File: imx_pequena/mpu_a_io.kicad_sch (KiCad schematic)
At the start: 12 parts, among them J1 Conn_ARM_JTAG_SWD_10, U1 MCIMX6Z0DVM09AB, Y1 Crystal, Y2 Crystal

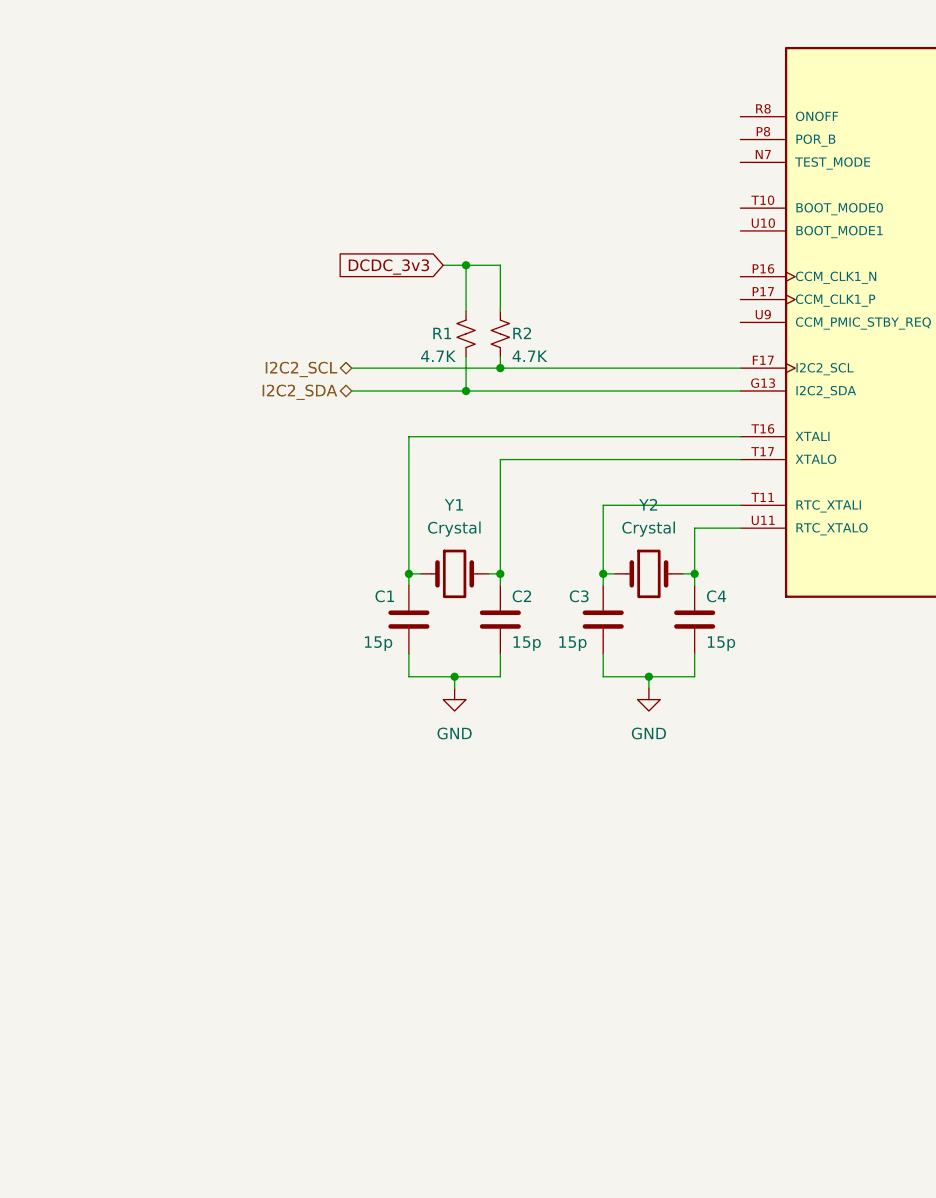
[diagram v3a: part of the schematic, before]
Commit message: Updated config
Updated config file and some pins
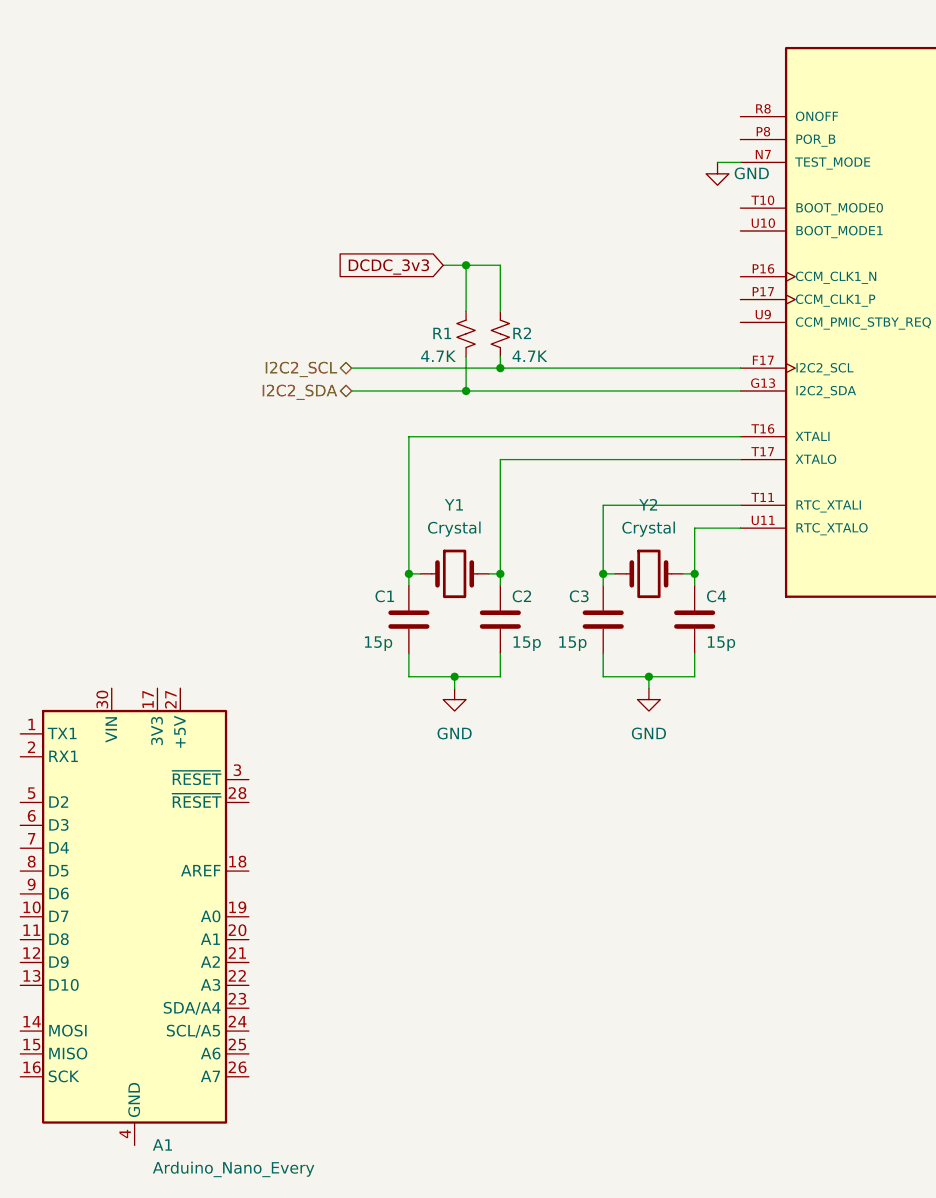
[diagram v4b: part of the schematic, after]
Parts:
- added A1: Arduino_Nano_Every, Module:Arduino_Nano, symbol MCU_Module:Arduino_Nano_Every
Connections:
- net GND: now also U1.N7 (TEST_MODE)
- new net: A1.29 (GND), A1.4 (GND)
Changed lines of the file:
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@@
+    (stroke (width 0) (type default) (color 0 0 0 0))
+  )
+  (wire (pts (xy 106.68 68.58) (xy 109.22 68.58))
     (stroke (width 0) (type default) (color 0 0 0 0))
   )
@@
     (pin "1")
     (pin "2")
+  )
+  (symbol (lib_id "MCU_Module:Arduino_Nano_Every") (at 41.91 152.4 0) (unit 1)
+    (in_bom yes) (on_board yes) (fields_autoplaced)
+    (property "Reference" "A1" (id 0) (at 43.9294 177.8 0)
+      (effects (font (size 1.27 1.27)) (justify left))
+    )
+    (property "Value" "Arduino_Nano_Every" (id 1) (at 43.9294 180.34 0)
+      (effects (font (size 1.27 1.27)) (justify left))
+    )
+    (property "Footprint" "Module:Arduino_Nano" (id 2) (at 41.91 152.4 0)
+      (effects (font (size 1.27 1.27) italic) hide)
+    )
+    (property "Datasheet" "https://content.arduino.cc/assets/NANOEveryV3.0_sch.pdf" (id 3) (at 41.91 152.4 0)
+      (effects (font (size 1.27 1.27)) hide)
+    )
+    (pin "1")
+    (pin "10")
+    (pin "11")
+    (pin "12")
+    (pin "13")
+    (pin "14")
+    (pin "15")
+    (pin "16")
+    (pin "17")
+    (pin "18")
+    (pin "19")
+    (pin "2")
+    (pin "20")
+    (pin "21")
+    (pin "22")
+    (pin "23")
+    (pin "24")
+    (pin "25")
+    (pin "26")
+    (pin "27")
+    (pin "28")
+    (pin "29")
+    (pin "3")
+    (pin "30")
+    (pin "4")
+    (pin "5")
+    (pin "6")
+    (pin "7")
+    (pin "8")
+    (pin "9")
   )
   (symbol (lib_id "power:GND") (at 77.47 127 0) (unit 1)
@@
     (pin "U9")
   )
+  (symbol (lib_id "power:GND") (at 106.68 68.58 0) (unit 1)
+    (in_bom yes) (on_board yes)
+    (property "Reference" "#PWR?" (id 0) (at 106.68 74.93 0)
+      (effects (font (size 1.27 1.27)) hide)
+    )
+    (property "Value" "GND" (id 1) (at 110.49 69.85 0))
+    (property "Footprint" "" (id 2) (at 106.68 68.58 0)
+      (effects (font (size 1.27 1.27)) hide)
+    )
+    (property "Datasheet" "" (id 3) (at 106.68 68.58 0)
+      (effects (font (size 1.27 1.27)) hide)
+    )
+    (pin "1")
+  )
   (symbol (lib_id "Device:R_Small_US") (at 82.55 87.63 0) (unit 1)

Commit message: Power upates
Added connections to power pins and decoupling caps
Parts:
- added C?: 10u, symbol Device:C_Small
- added C?: 0.22uF, symbol Device:C_Small
- added D?: D_Schottky, symbol Device:D_Schottky
- added R?: DNP, symbol Device:R_Small_US
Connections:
- net DCDC_3v3: now also D?.2 (A), R?.1
- net GND: now also C?.2, C?.2
- net at J1.1 (VTref): now also D?.1 (K), R?.2
- net at U1.P13 (NVCC_PLL): now also C?.1, C?.1
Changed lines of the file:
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@@
   (junction (at 78.74 80.01) (diameter 0) (color 0 0 0 0)
   )
+  (junction (at 199.39 58.42) (diameter 0) (color 0 0 0 0)
+  )
+  (junction (at 248.92 109.22) (diameter 0) (color 0 0 0 0)
+  )
   (junction (at 82.55 114.3) (diameter 0) (color 0 0 0 0)
   )
+  (junction (at 237.49 101.6) (diameter 0) (color 0 0 0 0)
+  )
   (junction (at 99.06 125.73) (diameter 0) (color 0 0 0 0)
   )
@@
   (junction (at 77.47 125.73) (diameter 0) (color 0 0 0 0)
   )
+  (wire (pts (xy 199.39 58.42) (xy 199.39 59.69))
+    (stroke (width 0) (type default) (color 0 0 0 0))
+  )
   (wire (pts (xy 185.42 114.3) (xy 187.96 114.3))
     (stroke (width 0) (type default) (color 0 0 0 0))
@@
     (stroke (width 0) (type default) (color 0 0 0 0))
   )
+  (wire (pts (xy 248.92 101.6) (xy 246.38 101.6))
+    (stroke (width 0) (type default) (color 0 0 0 0))
+  )
   (wire (pts (xy 93.98 114.3) (xy 93.98 115.57))
     (stroke (width 0) (type default) (color 0 0 0 0))
@@
     (stroke (width 0) (type default) (color 0 0 0 0))
   )
+  (wire (pts (xy 185.42 58.42) (xy 199.39 58.42))
+    (stroke (width 0) (type default) (color 0 0 0 0))
+  )
   (wire (pts (xy 104.14 109.22) (xy 109.22 109.22))
     (stroke (width 0) (type default) (color 0 0 0 0))
@@
     (stroke (width 0) (type default) (color 0 0 0 0))
   )
+  (wire (pts (xy 208.28 59.69) (xy 208.28 58.42))
+    (stroke (width 0) (type default) (color 0 0 0 0))
+  )
   (wire (pts (xy 247.65 17.78) (xy 247.65 20.32))
     (stroke (width 0) (type default) (color 0 0 0 0))
@@
     (stroke (width 0) (type default) (color 0 0 0 0))
   )
+  (wire (pts (xy 237.49 109.22) (xy 237.49 101.6))
+    (stroke (width 0) (type default) (color 0 0 0 0))
+  )
   (wire (pts (xy 247.65 27.94) (xy 247.65 30.48))
     (stroke (width 0) (type default) (color 0 0 0 0))
@@
     (stroke (width 0) (type default) (color 0 0 0 0))
   )
+  (wire (pts (xy 233.68 101.6) (xy 237.49 101.6))
+    (stroke (width 0) (type default) (color 0 0 0 0))
+  )
   (wire (pts (xy 72.39 114.3) (xy 72.39 115.57))
     (stroke (width 0) (type default) (color 0 0 0 0))
@@
     (stroke (width 0) (type default) (color 0 0 0 0))
   )
+  (wire (pts (xy 248.92 113.03) (xy 248.92 109.22))
+    (stroke (width 0) (type default) (color 0 0 0 0))
+  )
+  (wire (pts (xy 237.49 101.6) (xy 238.76 101.6))
+    (stroke (width 0) (type default) (color 0 0 0 0))
+  )
   (wire (pts (xy 72.39 125.73) (xy 72.39 123.19))
     (stroke (width 0) (type default) (color 0 0 0 0))
@@
     (stroke (width 0) (type default) (color 0 0 0 0))
   )
+  (wire (pts (xy 199.39 58.42) (xy 208.28 58.42))
+    (stroke (width 0) (type default) (color 0 0 0 0))
+  )
   (wire (pts (xy 82.55 125.73) (xy 82.55 123.19))
     (stroke (width 0) (type default) (color 0 0 0 0))
@@
     (stroke (width 0) (type default) (color 0 0 0 0))
   )
+  (wire (pts (xy 240.03 109.22) (xy 237.49 109.22))
+    (stroke (width 0) (type default) (color 0 0 0 0))
+  )
+  (wire (pts (xy 248.92 109.22) (xy 248.92 101.6))
+    (stroke (width 0) (type default) (color 0 0 0 0))
+  )
   (wire (pts (xy 265.43 27.94) (xy 265.43 30.48))
     (stroke (width 0) (type default) (color 0 0 0 0))
@@
     (stroke (width 0) (type default) (color 0 0 0 0))
   )
+  (wire (pts (xy 199.39 64.77) (xy 199.39 66.04))
+    (stroke (width 0) (type default) (color 0 0 0 0))
+  )
   (wire (pts (xy 73.66 114.3) (xy 72.39 114.3))
     (stroke (width 0) (type default) (color 0 0 0 0))
@@
     (stroke (width 0) (type default) (color 0 0 0 0))
   )
+  (wire (pts (xy 245.11 109.22) (xy 248.92 109.22))
+    (stroke (width 0) (type default) (color 0 0 0 0))
+  )
   (wire (pts (xy 82.55 85.09) (xy 82.55 80.01))
     (stroke (width 0) (type default) (color 0 0 0 0))
   )
   (wire (pts (xy 261.62 125.73) (xy 265.43 125.73))
+    (stroke (width 0) (type default) (color 0 0 0 0))
+  )
+  (wire (pts (xy 208.28 64.77) (xy 208.28 66.04))
     (stroke (width 0) (type default) (color 0 0 0 0))
   )
@@
     )
   )
+  (global_label "DCDC_3v3" (shape input) (at 233.68 101.6 180) (fields_autoplaced)
+    (effects (font (size 1.27 1.27)) (justify right))
+    (property "Intersheet References" "${INTERSHEET_REFS}" (id 0) (at 221.8326 101.5206 0)
+      (effects (font (size 1.27 1.27)) (justify right) hide)
+    )
+  )
   (hierarchical_label "USB1_VBUS" (shape bidirectional) (at 187.96 81.28 0)
     (effects (font (size 1.27 1.27)) (justify left))
@@
   (hierarchical_label "USB2_DN" (shape bidirectional) (at 187.96 83.82 0)
     (effects (font (size 1.27 1.27)) (justify left))
+  )
+  (symbol (lib_id "power:GND") (at 199.39 66.04 0) (unit 1)
+    (in_bom yes) (on_board yes) (fields_autoplaced)
+    (property "Reference" "#PWR?" (id 0) (at 199.39 72.39 0)
+      (effects (font (size 1.27 1.27)) hide)
+    )
+    (property "Value" "GND" (id 1) (at 199.39 71.12 0))
+    (property "Footprint" "" (id 2) (at 199.39 66.04 0)
+      (effects (font (size 1.27 1.27)) hide)
+    )
+    (property "Datasheet" "" (id 3) (at 199.39 66.04 0)
+      (effects (font (size 1.27 1.27)) hide)
+    )
+    (pin "1")
   )
   (symbol (lib_id "power:GND") (at 99.06 127 0) (unit 1)
@@
     (pin "1")
     (pin "2")
+  )
+  (symbol (lib_id "power:GND") (at 208.28 66.04 0) (unit 1)
+    (in_bom yes) (on_board yes) (fields_autoplaced)
+    (property "Reference" "#PWR?" (id 0) (at 208.28 72.39 0)
+      (effects (font (size 1.27 1.27)) hide)
+    )
+    (property "Value" "GND" (id 1) (at 208.28 71.12 0))
+    (property "Footprint" "" (id 2) (at 208.28 66.04 0)
+      (effects (font (size 1.27 1.27)) hide)
+    )
+    (property "Datasheet" "" (id 3) (at 208.28 66.04 0)
+      (effects (font (size 1.27 1.27)) hide)
+    )
+    (pin "1")
   )
   (symbol (lib_id "MCU_Module:Arduino_Nano_Every") (at 41.91 152.4 0) (unit 1)
@@
     (pin "2")
   )
+  (symbol (lib_id "Device:C_Small") (at 208.28 62.23 0) (unit 1)
+    (in_bom yes) (on_board yes)
+    (property "Reference" "C?" (id 0) (at 209.55 60.96 0)
+      (effects (font (size 1.27 1.27)) (justify left))
+    )
+    (property "Value" "10u" (id 1) (at 209.55 64.77 0)
+      (effects (font (size 1.27 1.27)) (justify left))
+    )
+    (property "Footprint" "" (id 2) (at 208.28 62.23 0)
+      (effects (font (size 1.27 1.27)) hide)
+    )
+    (property "Datasheet" "~" (id 3) (at 208.28 62.23 0)
+      (effects (font (size 1.27 1.27)) hide)
+    )
+    (pin "1")
+    (pin "2")
+  )
   (symbol (lib_id "power:GND") (at 265.43 30.48 0) (unit 1)
     (in_bom yes) (on_board yes) (fields_autoplaced)
@@
     (pin "9")
   )
+  (symbol (lib_id "Device:C_Small") (at 199.39 62.23 0) (unit 1)
+    (in_bom yes) (on_board yes)
+    (property "Reference" "C?" (id 0) (at 200.66 60.96 0)
+      (effects (font (size 1.27 1.27)) (justify left))
+    )
+    (property "Value" "0.22uF" (id 1) (at 199.39 64.77 0)
+      (effects (font (size 1.27 1.27)) (justify left))
+    )
+    (property "Footprint" "" (id 2) (at 199.39 62.23 0)
+      (effects (font (size 1.27 1.27)) hide)
+    )
+    (property "Datasheet" "~" (id 3) (at 199.39 62.23 0)
+      (effects (font (size 1.27 1.27)) hide)
+    )
+    (pin "1")
+    (pin "2")
+  )
   (symbol (lib_id "Device:C") (at 93.98 119.38 0) (unit 1)
     (in_bom yes) (on_board yes)
@@
       (effects (font (size 1.27 1.27)) hide)
     )
+    (pin "1")
+    (pin "2")
+  )
+  (symbol (lib_id "Device:R_Small_US") (at 242.57 109.22 90) (unit 1)
+    (in_bom yes) (on_board yes)
+    (property "Reference" "R?" (id 0) (at 240.03 107.95 90))
+    (property "Value" "DNP" (id 1) (at 245.11 107.95 90))
+    (property "Footprint" "" (id 2) (at 242.57 109.22 0)
+      (effects (font (size 1.27 1.27)) hide)
+    )
+    (property "Datasheet" "~" (id 3) (at 242.57 109.22 0)
+      (effects (font (size 1.27 1.27)) hide)
+    )
+    (pin "1")
+    (pin "2")
+  )
+  (symbol (lib_id "Device:D_Schottky") (at 242.57 101.6 180) (unit 1)
+    (in_bom yes) (on_board yes) (fields_autoplaced)
+    (property "Reference" "D?" (id 0) (at 242.8875 95.25 0))
+    (property "Value" "D_Schottky" (id 1) (at 242.8875 97.79 0))
+    (property "Footprint" "" (id 2) (at 242.57 101.6 0)
+      (effects (font (size 1.27 1.27)) hide)
+    )
+    (property "Datasheet" "~" (id 3) (at 242.57 101.6 0)
+      (effects (font (size 1.27 1.27)) hide)
+    )

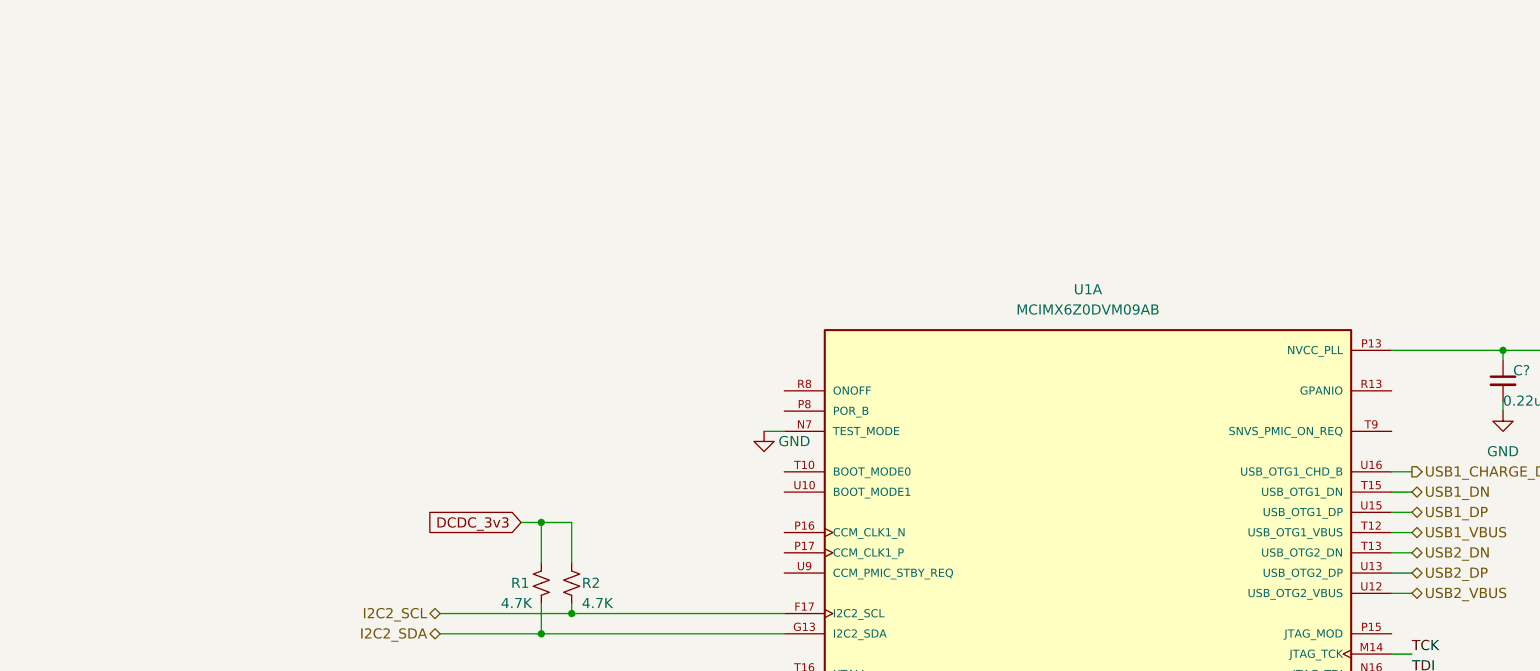
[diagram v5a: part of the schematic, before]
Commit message: Updated reset pins
Updated reset pins
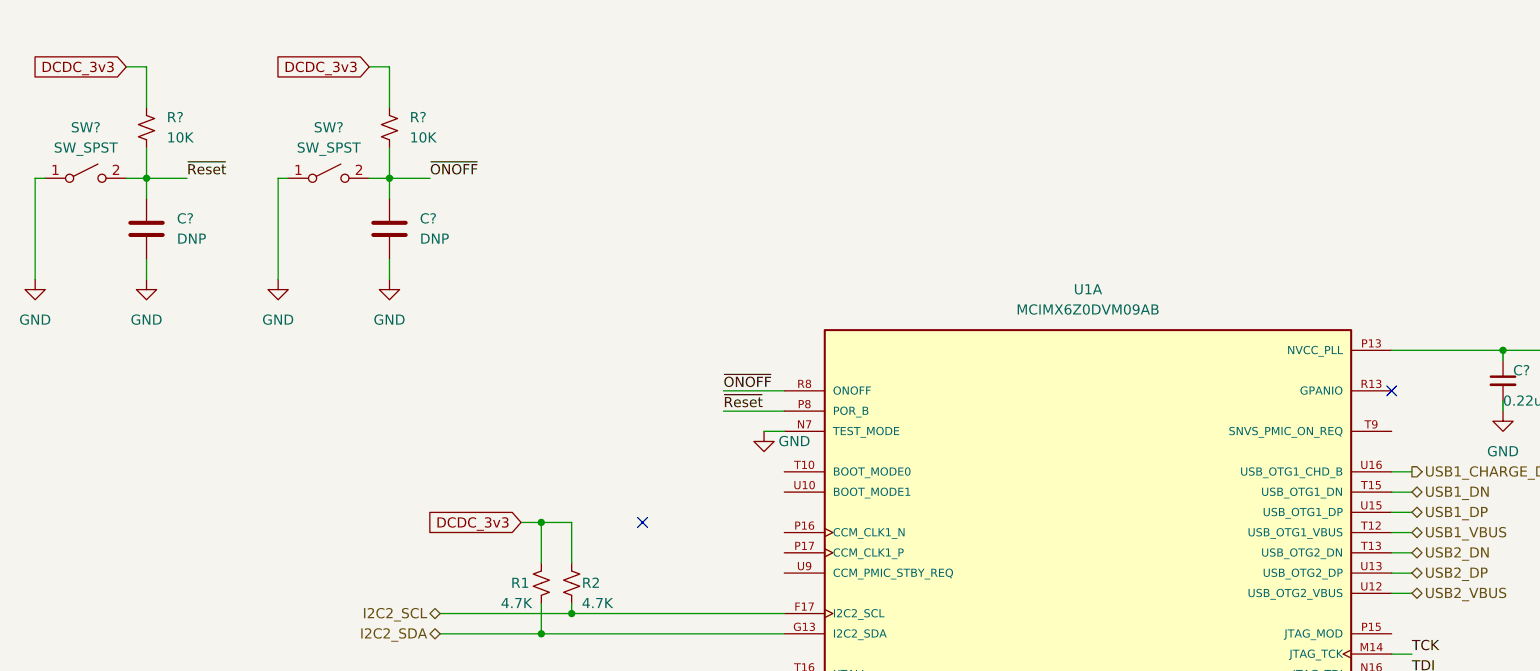
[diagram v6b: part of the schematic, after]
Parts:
- added C? (x2): DNP, symbol Device:C
- added R? (x2): 10K, symbol Device:R_Small_US
- added SW? (x2): SW_SPST, symbol Switch:SW_SPST
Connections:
- net DCDC_3v3: now also R?.1, R?.1
- net GND: now also C?.2, C?.2, SW?.1 (A), SW?.1 (A)
- net ~{Reset}: now reaches U1.P8 (POR_B)
- net ~{Reset}: now also C?.1, R?.2, SW?.2 (B)
- net ~{ONOFF}: now reaches U1.R8 (ONOFF)
- net ~{ONOFF}: now also C?.1, R?.2, SW?.2 (B)
- no-connect marks 0 -> 2
